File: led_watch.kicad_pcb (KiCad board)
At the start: 2 copper layers, 38 x 38 mm, 87 parts, among them J1 Conn_01x02, J2 Conn_01x02, SW1 SW_Push, U1 ATMEGA328P-AU, U2 MCP7940N, Y1 16MHz, Y2 32.768kHz

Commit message: "holy s#@% it's friday" commit
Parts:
- removed BT1: Battery_Cell, Battery_Holders:Keystone_1058_1x2032-CoinCell
- added J3: Conn_01x02, Pin_Headers:Pin_Header_Straight_1x02_Pitch1.00mm, F.Cu at (141.5, 105.7)
- moved R7 0.76 mm to (144.5, 107.2)
- moved R8 0.76 mm to (146.1, 107.2)
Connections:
- net Net-(BT1-Pad1) renamed /VCC
- C3 pad 2: GND -> Net-(C3-Pad2)
- C4 pad 1: GND -> Net-(C3-Pad2)
- R1 pad 1: Net-(R1-Pad1) -> Net-(C3-Pad2)
- SW1 pad 2: Net-(R1-Pad1) -> Net-(C3-Pad2)
- U1 pad 13: Net-(R1-Pad1) -> Net-(C3-Pad2)
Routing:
- net Net-(C3-Pad2): track 0.00 -> 35.5 mm, vias 0 -> 3
- net Net-(R1-Pad1): track 18.6 -> 0.00 mm, vias 2 -> 0
- net /VCC: track 53.7 -> 66.3 mm
- net GND: track 62.0 -> 57.8 mm
- net Net-(R7-Pad2): track 2.73 -> 3.35 mm

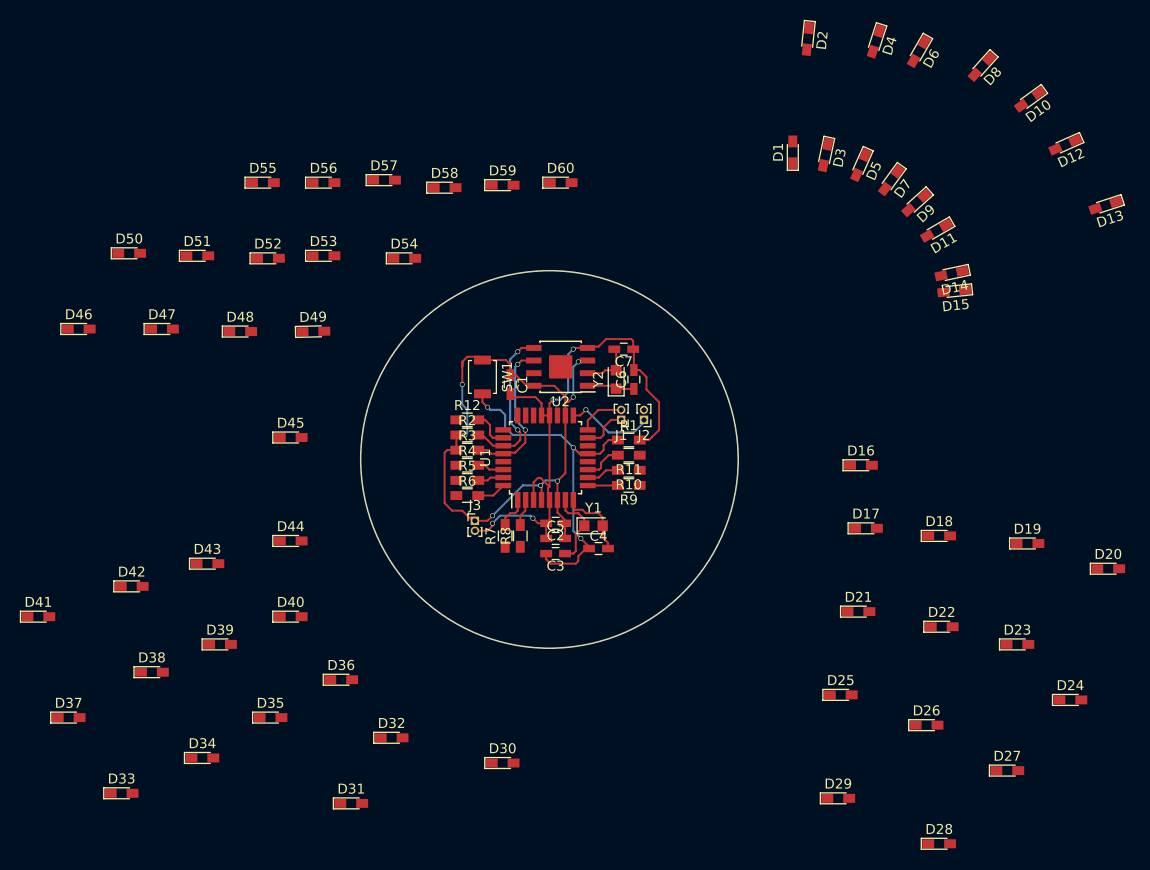
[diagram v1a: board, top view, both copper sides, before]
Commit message: wiring
started wiring up the outside leds. this is difficult.
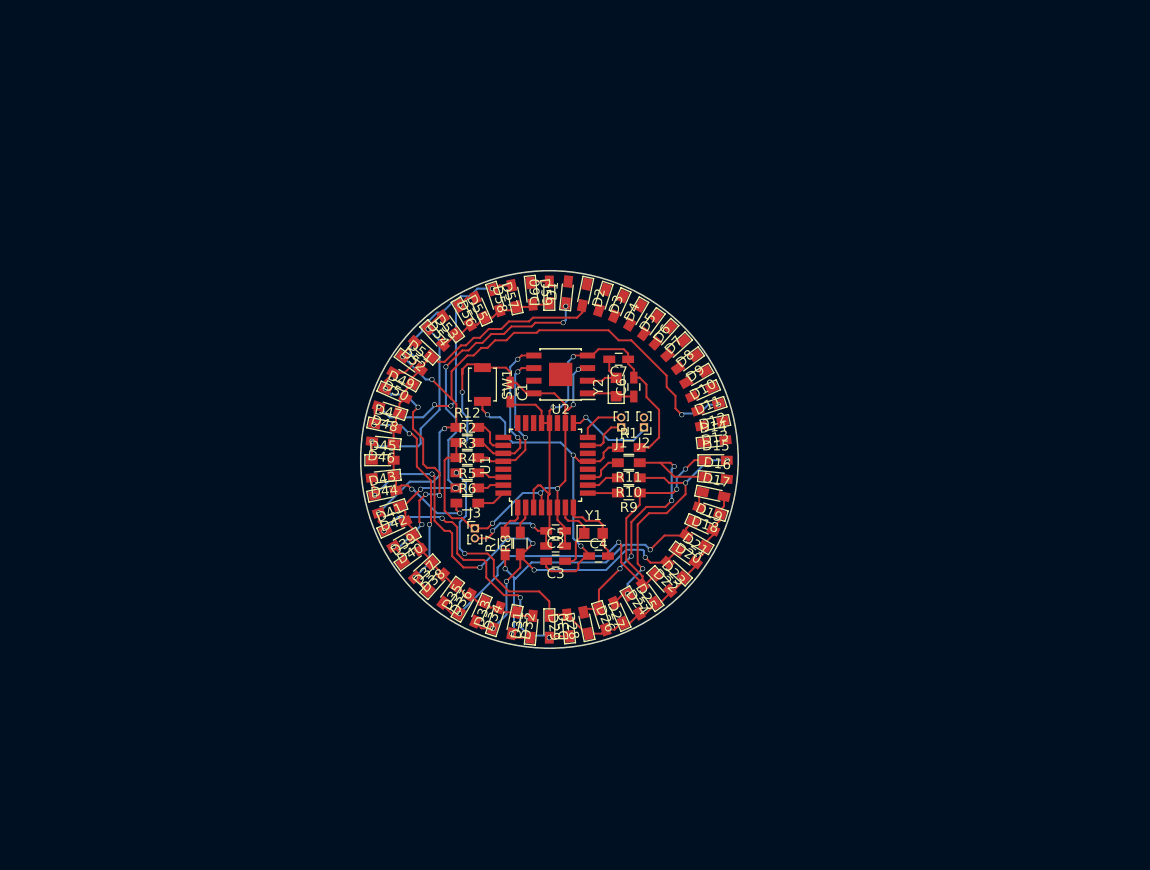
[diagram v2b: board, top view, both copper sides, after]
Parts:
- moved D13 45.3 mm to (165.4, 95.9), turned to 192 degrees
- moved D12 44.6 mm to (165.0, 94.2), turned to 198 degrees
- moved D10 43.7 mm to (163.7, 91.2), turned to 210 degrees
- moved D24 43.7 mm to (159.0, 113.0), turned to 126 degrees
- moved D27 43.5 mm to (154.3, 115.6), turned to 288 degrees
- moved D28 41.9 mm to (152.7, 116.0), turned to 102 degrees
- moved D8 41.9 mm to (161.7, 88.3), turned to 222 degrees
- moved D33 41.6 mm to (143.6, 115.4), turned to 72 degrees
- moved D20 41.6 mm to (163.7, 107.7), turned to 150 degrees
- moved D37 39.4 mm to (137.5, 111.9), turned to 48 degrees
- moved D6 38.6 mm to (159.1, 86.0), turned to 234 degrees
- moved D4 37.2 mm to (156.0, 84.1), turned to 246 degrees
- moved D41 37.1 mm to (133.5, 106.2), turned to 24 degrees
- moved D23 36.2 mm to (160.4, 111.9), turned to 312 degrees
- moved D2 34.2 mm to (152.5, 82.9), turned to 258 degrees
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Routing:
- net Net-(D12-Pad1): track 0.00 -> 95.1 mm, vias 0 -> 10
- net Net-(D12-Pad2): track 0.00 -> 74.5 mm, vias 0 -> 12
- net Net-(D11-Pad1): track 0.00 -> 72.0 mm, vias 0 -> 12
- net Net-(D11-Pad2): track 0.00 -> 70.5 mm, vias 0 -> 6
- net Net-(D10-Pad1): track 0.00 -> 59.4 mm, vias 0 -> 8
- net Net-(D1-Pad1): track 0.00 -> 54.9 mm, vias 0 -> 6
- net Net-(D1-Pad2): track 0.00 -> 49.3 mm, vias 0 -> 2
- net Net-(D10-Pad2): track 0.00 -> 44.2 mm, vias 0 -> 3
- net Net-(D13-Pad2): track 0.00 -> 44.0 mm, vias 0 -> 2
- net GND: track 57.8 -> 57.0 mm
